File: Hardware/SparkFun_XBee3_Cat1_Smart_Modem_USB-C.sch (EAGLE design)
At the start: 53 parts, among them J3 USB Female Type C Connector, J4 QWIIC_RIGHT_ANGLE, U2 AP63203, U5 ESD Diode, U7 FT231XS

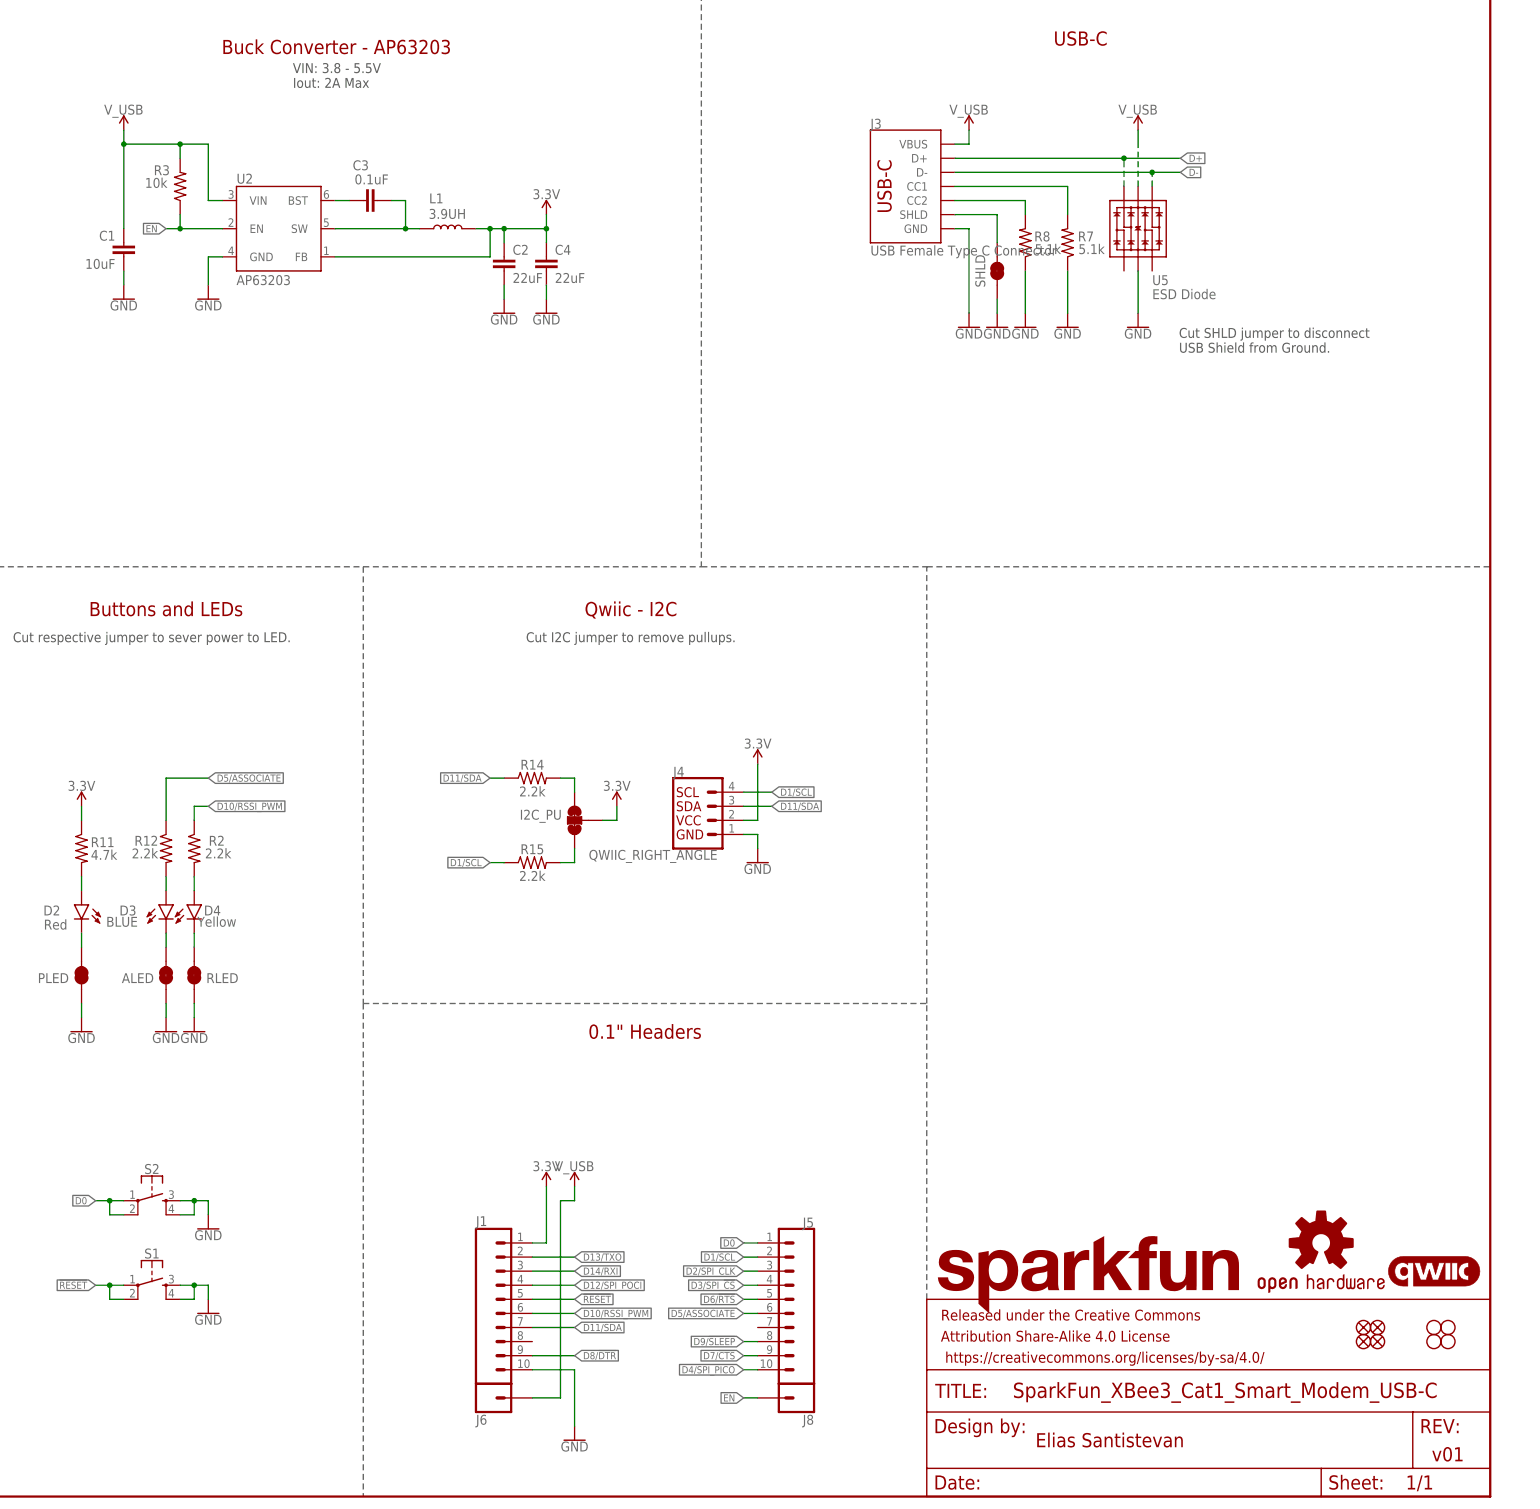
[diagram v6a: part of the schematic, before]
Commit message: Adds many GND vias
* Adds ordering instructions
* Changes VUSB net to VIN for consistency with other Xbee products
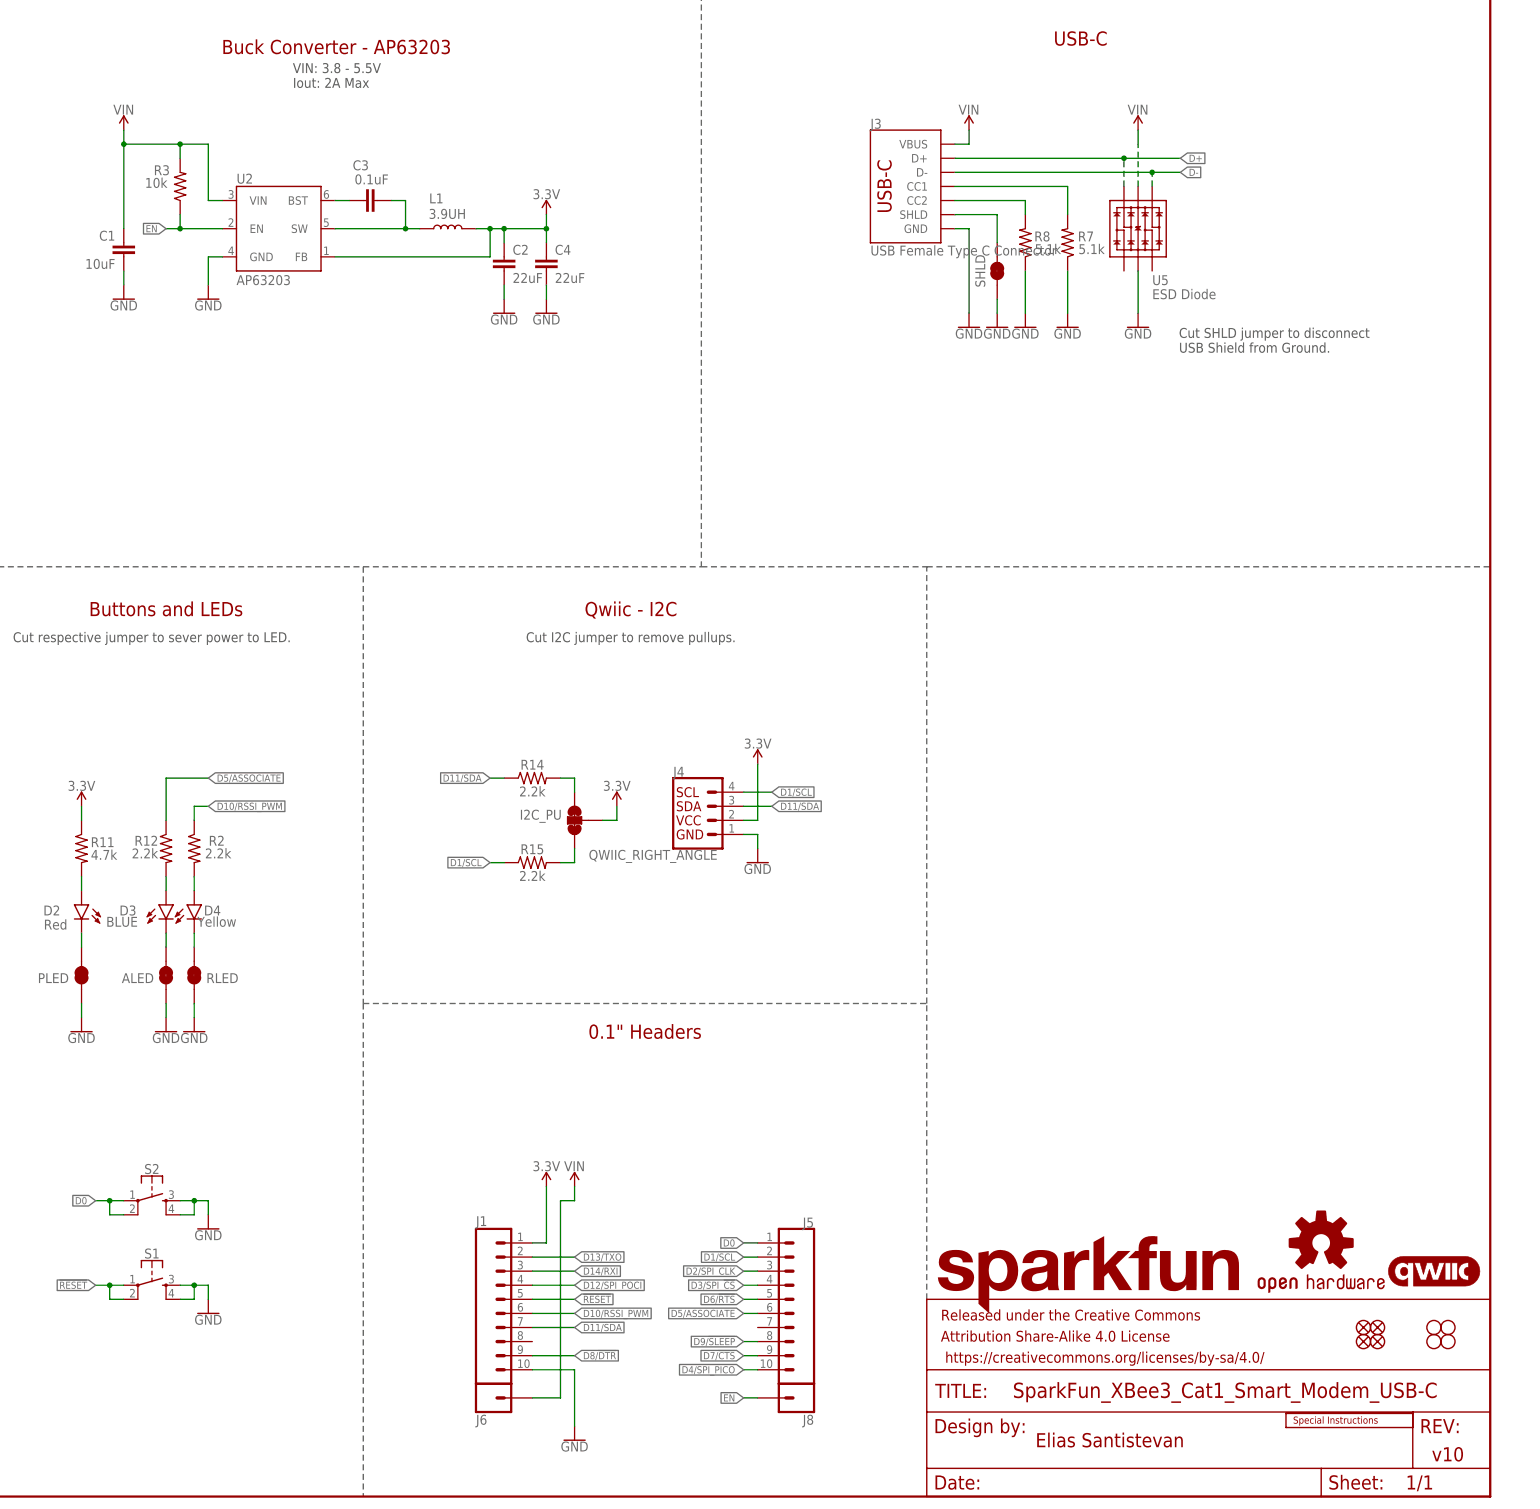
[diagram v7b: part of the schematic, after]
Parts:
- added LOGO4: SPECIAL_INSTRUCTIONS-ORDERING, SparkFun-Aesthetics:SPECIAL_INSTRUCTIONS-ORDERING
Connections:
- net V_USB renamed VIN
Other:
- note added: "v10"
- note removed: "v01"
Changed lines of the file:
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@@
 <part name="SHLD" library="SparkFun-Jumpers" deviceset="JUMPER-SMT_2_NC_TRACE" device="_SILK" package3d_urn="urn:adsk.eagle:package:39281/1"/>
 <part name="GND19" library="SparkFun-PowerSymbols" deviceset="GND" device=""/>
-<part name="SUPPLY9" library="SparkFun-PowerSymbols" deviceset="V_USB" device=""/>
+<part name="SUPPLY9" library="SparkFun-PowerSymbols" deviceset="VIN" device=""/>
 <part name="U5" library="SparkFun-DiscreteSemi" deviceset="TVS_DIODE_ARRAY" device="_DT1042-04SO-7" value="ESD Diode"/>
 <part name="GND27" library="SparkFun-PowerSymbols" deviceset="GND" device=""/>
-<part name="SUPPLY16" library="SparkFun-PowerSymbols" deviceset="V_USB" device=""/>
+<part name="SUPPLY16" library="SparkFun-PowerSymbols" deviceset="VIN" device=""/>
 <part name="FRAME1" library="SparkFun-Aesthetics" deviceset="FRAME-LEDGER" device=""/>
 <part name="U7" library="SparkFun-IC-Comms" deviceset="FT231X" device="S" value="FT231XS"/>
@@
 <part name="J1" library="SparkFun-Connectors" deviceset="CONN_01" device="PTH_NO_SILK_STAND"/>
 <part name="J8" library="SparkFun-Connectors" deviceset="CONN_01" device="PTH_NO_SILK_STAND"/>
-<part name="SUPPLY5" library="SparkFun-PowerSymbols" deviceset="V_USB" device=""/>
-<part name="SUPPLY11" library="SparkFun-PowerSymbols" deviceset="V_USB" device=""/>
+<part name="SUPPLY5" library="SparkFun-PowerSymbols" deviceset="VIN" device=""/>
+<part name="SUPPLY11" library="SparkFun-PowerSymbols" deviceset="VIN" device=""/>
 <part name="LOGO1" library="SparkFun-Aesthetics" deviceset="SFE_LOGO_NAME" device=".2_INCH"/>
+<part name="LOGO4" library="SparkFun-Aesthetics" deviceset="SPECIAL_INSTRUCTIONS" device="-ORDERING"/>
 </parts>
 <sheets>
@@
 <text x="223.774" y="261.366" size="2.54" layer="94" font="vector" align="center">Buck Converter - AP63203</text>
 <text x="276.86" y="160.02" size="2.54" layer="94" font="vector" align="center">Qwiic - I2C</text>
-<text x="424.18" y="7.62" size="2.54" layer="94" font="vector" align="center">v01</text>
+<text x="424.18" y="7.62" size="2.54" layer="94" font="vector" align="center">v10</text>
 <text x="363.22" y="10.16" size="2.54" layer="94" font="vector" align="center">Elias Santistevan</text>
 <text x="193.04" y="160.02" size="2.54" layer="94" font="vector" align="center">Buttons and LEDs</text>
@@
 </instance>
 <instance part="LOGO1" gate="G$1" x="330.2" y="33.02" smashed="yes"/>
+<instance part="LOGO4" gate="G$1" x="394.97" y="12.446" smashed="yes"/>
 </instances>
 <busses>
@@
 </segment>
 </net>
-<net name="V_USB" class="0">
-<segment>
-<pinref part="J3" gate="J1" pin="VBUS"/>
-<wire x1="335.28" y1="243.84" x2="337.82" y2="243.84" width="0.1524" layer="91"/>
-<wire x1="337.82" y1="246.38" x2="337.82" y2="243.84" width="0.1524" layer="91"/>
-<pinref part="SUPPLY9" gate="G$1" pin="V_USB"/>
-</segment>
-<segment>
-<pinref part="U5" gate="U1" pin="VCC"/>
-<wire x1="368.3" y1="236.22" x2="368.3" y2="243.84" width="0.1524" layer="91" style="longdash"/>
-<pinref part="SUPPLY16" gate="G$1" pin="V_USB"/>
-<wire x1="368.3" y1="243.84" x2="368.3" y2="246.38" width="0.1524" layer="91"/>
-</segment>
-<segment>
-<wire x1="185.42" y1="246.38" x2="185.42" y2="243.84" width="0.1524" layer="91"/>
+<net name="N$5" class="0">
+<segment>
+<pinref part="J3" gate="J1" pin="CC2"/>
+<wire x1="335.28" y1="233.68" x2="347.98" y2="233.68" width="0.1524" layer="91"/>
+<wire x1="347.98" y1="233.68" x2="347.98" y2="231.14" width="0.1524" layer="91"/>
+<pinref part="R8" gate="R1" pin="2"/>
+</segment>
+</net>
+<net name="N$6" class="0">
+<segment>
+<pinref part="J3" gate="J1" pin="CC1"/>
+<wire x1="335.28" y1="236.22" x2="355.6" y2="236.22" width="0.1524" layer="91"/>
+<wire x1="355.6" y1="236.22" x2="355.6" y2="231.14" width="0.1524" layer="91"/>
+<pinref part="R7" gate="R1" pin="2"/>
+</segment>
+</net>
+<net name="SHLD" class="0">
+<segment>
+<pinref part="J3" gate="J1" pin="SHLD"/>
+<wire x1="335.28" y1="231.14" x2="342.9" y2="231.14" width="0.1524" layer="91"/>
+<wire x1="342.9" y1="231.14" x2="342.9" y2="226.06" width="0.1524" layer="91"/>
+<pinref part="SHLD" gate="G$1" pin="2"/>
+</segment>
+</net>
+<net name="D+" class="2">
+<segment>
+<pinref part="J3" gate="J1" pin="D+"/>
+<wire x1="335.28" y1="241.3" x2="365.76" y2="241.3" width="0.1524" layer="91"/>
+<label x="375.92" y="241.3" size="1.27" layer="95" font="vector" xref="yes"/>
+<pinref part="U5" gate="U1" pin="IO4"/>
+<wire x1="365.76" y1="241.3" x2="375.92" y2="241.3" width="0.1524" layer="91"/>
+<wire x1="365.76" y1="236.22" x2="365.76" y2="241.3" width="0.1524" layer="91" style="longdash"/>
+<junction x="365.76" y="241.3"/>
+</segment>
+<segment>
+<wire x1="78.74" y1="101.6" x2="73.66" y2="101.6" width="0.1524" layer="91"/>
+<label x="73.66" y="101.6" size="1.27" layer="95" font="vector" rot="R180" xref="yes"/>
+<pinref part="U7" gate="U$1" pin="USBDP"/>
+</segment>
+</net>
+<net name="D-" class="2">
+<segment>
+<pinref part="J3" gate="J1" pin="D-"/>
+<wire x1="375.92" y1="238.76" x2="370.84" y2="238.76" width="0.1524" layer="91"/>
+<label x="375.92" y="238.76" size="1.27" layer="95" font="vector" xref="yes"/>
+<pinref part="U5" gate="U1" pin="IO3"/>
+<wire x1="370.84" y1="238.76" x2="335.28" y2="238.76" width="0.1524" layer="91"/>
+<wire x1="370.84" y1="236.22" x2="370.84" y2="238.76" width="0.1524" layer="91" style="longdash"/>
+<junction x="370.84" y="238.76"/>
+</segment>
+<segment>
+<wire x1="78.74" y1="104.14" x2="73.66" y2="104.14" width="0.1524" layer="91"/>
+<label x="73.66" y="104.14" size="1.27" layer="95" font="vector" rot="R180" xref="yes"/>
+<pinref part="U7" gate="U$1" pin="USBDM"/>
+</segment>
+</net>
+<net name="VIN" class="0">
+<segment>
 <pinref part="U2" gate="G$1" pin="VIN"/>
 <wire x1="203.2" y1="233.68" x2="200.66" y2="233.68" width="0.1524" layer="91"/>
@@
 <wire x1="195.58" y1="241.3" x2="195.58" y2="243.84" width="0.1524" layer="91"/>
 <junction x="195.58" y="243.84"/>
+<pinref part="SUPPLY5" gate="G$1" pin="VIN"/>
+<wire x1="185.42" y1="246.38" x2="185.42" y2="243.84" width="0.1524" layer="91"/>
 <junction x="185.42" y="243.84"/>
-<pinref part="SUPPLY5" gate="G$1" pin="V_USB"/>
+</segment>
+<segment>
+<pinref part="U5" gate="U1" pin="VCC"/>
+<wire x1="368.3" y1="236.22" x2="368.3" y2="243.84" width="0.1524" layer="91" style="longdash"/>
+<pinref part="SUPPLY16" gate="G$1" pin="VIN"/>
+<wire x1="368.3" y1="243.84" x2="368.3" y2="246.38" width="0.1524" layer="91"/>
+</segment>
+<segment>
+<pinref part="J3" gate="J1" pin="VBUS"/>
+<wire x1="335.28" y1="243.84" x2="337.82" y2="243.84" width="0.1524" layer="91"/>
+<pinref part="SUPPLY9" gate="G$1" pin="VIN"/>
+<wire x1="337.82" y1="246.38" x2="337.82" y2="243.84" width="0.1524" layer="91"/>
 </segment>
 <segment>
@@
 <pinref part="J1" gate="G$1" pin="1"/>
 <wire x1="264.16" y1="53.34" x2="266.7" y2="53.34" width="0.1524" layer="91"/>
-<wire x1="266.7" y1="53.34" x2="266.7" y2="55.88" width="0.1524" layer="91"/>
-<pinref part="SUPPLY11" gate="G$1" pin="V_USB"/>
-</segment>
-</net>
-<net name="N$5" class="0">
-<segment>
-<pinref part="J3" gate="J1" pin="CC2"/>
-<wire x1="335.28" y1="233.68" x2="347.98" y2="233.68" width="0.1524" layer="91"/>
-<wire x1="347.98" y1="233.68" x2="347.98" y2="231.14" width="0.1524" layer="91"/>
-<pinref part="R8" gate="R1" pin="2"/>
-</segment>
-</net>
-<net name="N$6" class="0">
-<segment>
-<pinref part="J3" gate="J1" pin="CC1"/>
-<wire x1="335.28" y1="236.22" x2="355.6" y2="236.22" width="0.1524" layer="91"/>
-<wire x1="355.6" y1="236.22" x2="355.6" y2="231.14" width="0.1524" layer="91"/>
-<pinref part="R7" gate="R1" pin="2"/>
-</segment>
-</net>
-<net name="SHLD" class="0">
-<segment>
-<pinref part="J3" gate="J1" pin="SHLD"/>
-<wire x1="335.28" y1="231.14" x2="342.9" y2="231.14" width="0.1524" layer="91"/>
-<wire x1="342.9" y1="231.14" x2="342.9" y2="226.06" width="0.1524" layer="91"/>
-<pinref part="SHLD" gate="G$1" pin="2"/>
-</segment>
-</net>
-<net name="D+" class="2">
-<segment>
-<pinref part="J3" gate="J1" pin="D+"/>
-<wire x1="335.28" y1="241.3" x2="365.76" y2="241.3" width="0.1524" layer="91"/>
-<label x="375.92" y="241.3" size="1.27" layer="95" font="vector" xref="yes"/>
-<pinref part="U5" gate="U1" pin="IO4"/>
-<wire x1="365.76" y1="241.3" x2="375.92" y2="241.3" width="0.1524" layer="91"/>
-<wire x1="365.76" y1="236.22" x2="365.76" y2="241.3" width="0.1524" layer="91" style="longdash"/>
-<junction x="365.76" y="241.3"/>
-</segment>
-<segment>
-<wire x1="78.74" y1="101.6" x2="73.66" y2="101.6" width="0.1524" layer="91"/>
-<label x="73.66" y="101.6" size="1.27" layer="95" font="vector" rot="R180" xref="yes"/>
-<pinref part="U7" gate="U$1" pin="USBDP"/>
-</segment>
-</net>
-<net name="D-" class="2">
-<segment>
-<pinref part="J3" gate="J1" pin="D-"/>
-<wire x1="375.92" y1="238.76" x2="370.84" y2="238.76" width="0.1524" layer="91"/>
-<label x="375.92" y="238.76" size="1.27" layer="95" font="vector" xref="yes"/>
-<pinref part="U5" gate="U1" pin="IO3"/>
-<wire x1="370.84" y1="238.76" x2="335.28" y2="238.76" width="0.1524" layer="91"/>
-<wire x1="370.84" y1="236.22" x2="370.84" y2="238.76" width="0.1524" layer="91" style="longdash"/>
-<junction x="370.84" y="238.76"/>
-</segment>
-<segment>
-<wire x1="78.74" y1="104.14" x2="73.66" y2="104.14" width="0.1524" layer="91"/>
-<label x="73.66" y="104.14" size="1.27" layer="95" font="vector" rot="R180" xref="yes"/>
-<pinref part="U7" gate="U$1" pin="USBDM"/>
-</segment>
-</net>
+<pinref part="SUPPLY11" gate="G$1" pin="VIN"/>
+<wire x1="266.7" y1="55.88" x2="266.7" y2="53.34" width="0.1524" layer="91"/>
+</segment>
+</net>

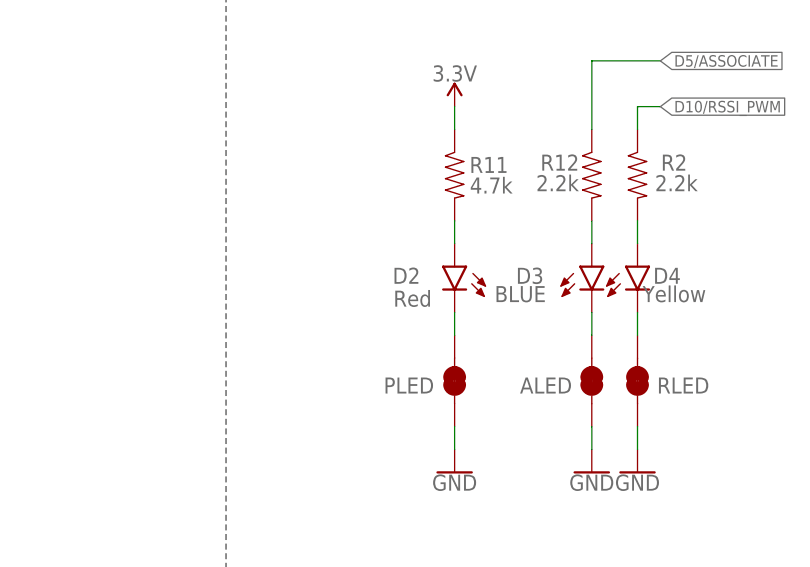
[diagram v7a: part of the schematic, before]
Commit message: Approves various DRC issues
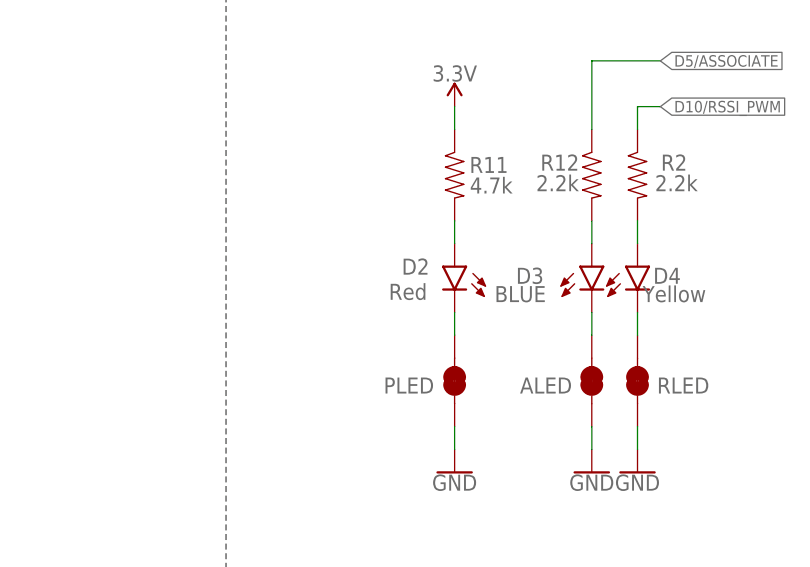
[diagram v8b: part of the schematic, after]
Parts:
- D2: device SparkFun-LED:LED-RED-0603-WE -> SparkFun-LED:LED-RED_0603-KB
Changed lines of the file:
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@@
 <part name="J6" library="SparkFun-Connectors" deviceset="CONN_10" device="NO_SILK_PTH_FEMALE"/>
 <part name="R11" library="SparkFun-Resistors" deviceset="4.7KOHM" device="-0603-1/10W-1%" value="4.7k"/>
-<part name="D2" library="SparkFun-LED" deviceset="LED-RED" device="-0603-WE" value="Red"/>
+<part name="D2" library="SparkFun-LED" deviceset="LED-RED" device="_0603-KB" value="Red"/>
 <part name="GND12" library="SparkFun-PowerSymbols" deviceset="GND" device=""/>
 <part name="SUPPLY8" library="SparkFun-PowerSymbols" deviceset="3.3V" device=""/>
@@
 </instance>
 <instance part="D2" gate="G$1" x="177.8" y="106.68" smashed="yes" rot="MR0">
-<attribute name="NAME" x="173.99" y="104.775" size="1.778" layer="95" font="vector" rot="MR0"/>
-<attribute name="VALUE" x="175.26" y="104.013" size="1.778" layer="96" font="vector" rot="MR0" align="top-left"/>
+<attribute name="NAME" x="175.006" y="105.791" size="1.778" layer="95" font="vector" rot="MR0"/>
+<attribute name="VALUE" x="174.752" y="104.775" size="1.778" layer="96" font="vector" rot="MR0" align="top-left"/>
 </instance>
 <instance part="GND12" gate="1" x="177.8" y="83.82" smashed="yes">
